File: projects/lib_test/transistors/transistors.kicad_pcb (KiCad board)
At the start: 2 copper layers, 21 x 16 mm, 4 parts, among them Q1001 MMBT2222A, Q1002 AO3400A, Q1003 DMP3028LFDE, Q1004 CEM3083

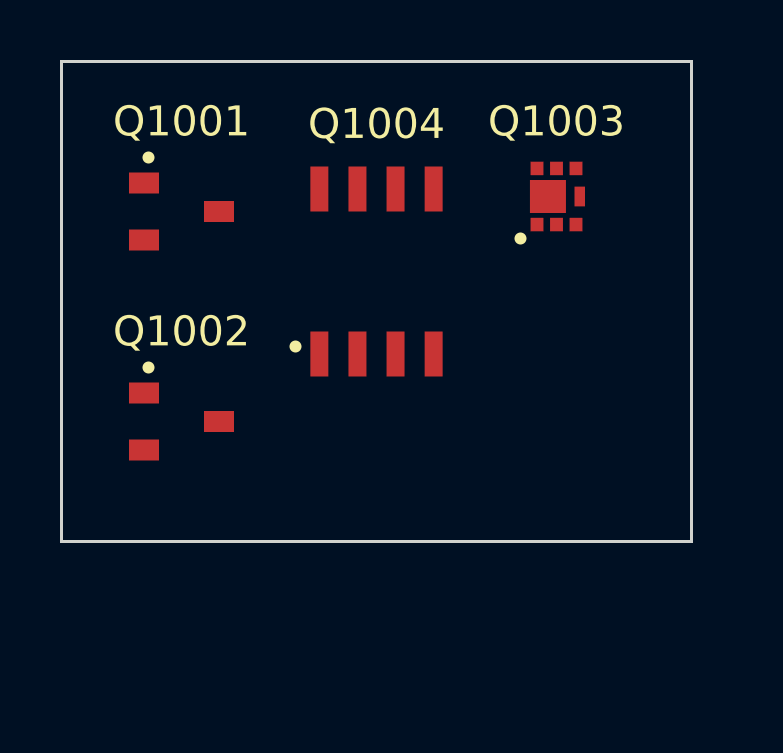
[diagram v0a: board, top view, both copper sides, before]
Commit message: add MOSFET N channel in SOIC8
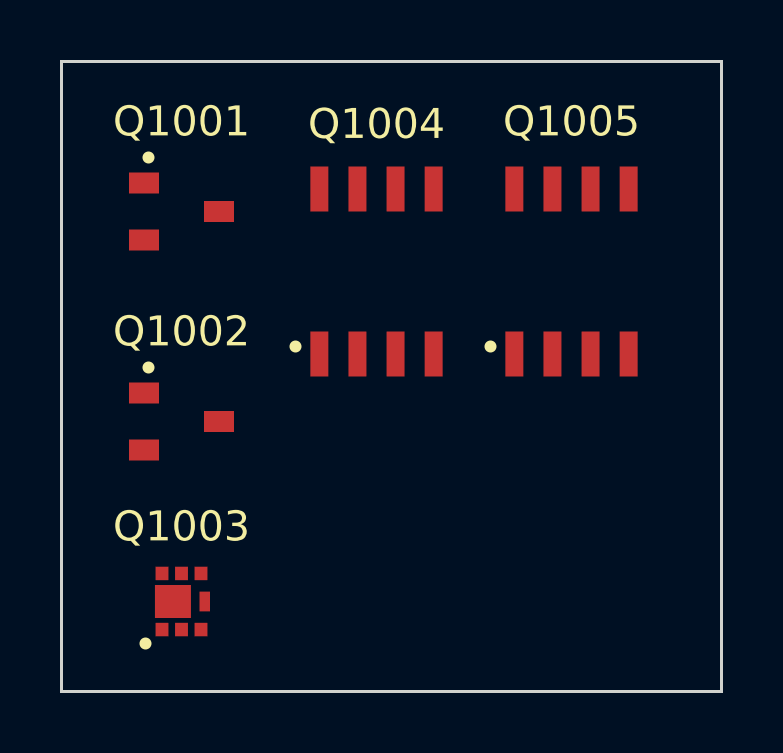
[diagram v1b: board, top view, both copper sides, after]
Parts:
- added Q1005: mosfet_n_8p_soic8, lily_footprints:soic8, F.Cu at (127.0, 77.0)
- moved Q1003 18.4 mm to (114.0, 88.0)
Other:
- board size 21 x 16 mm -> 22 x 21 mm

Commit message: updated value of N channel MOSFET
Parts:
- Q1005: value mosfet_n_8p_soic8 -> VBZA4800
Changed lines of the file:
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@@
 			)
 		)
-		(property "Value" "mosfet_n_8p_soic8"
+		(property "Value" "VBZA4800"
 			(at 0 0 0)
 			(unlocked yes)

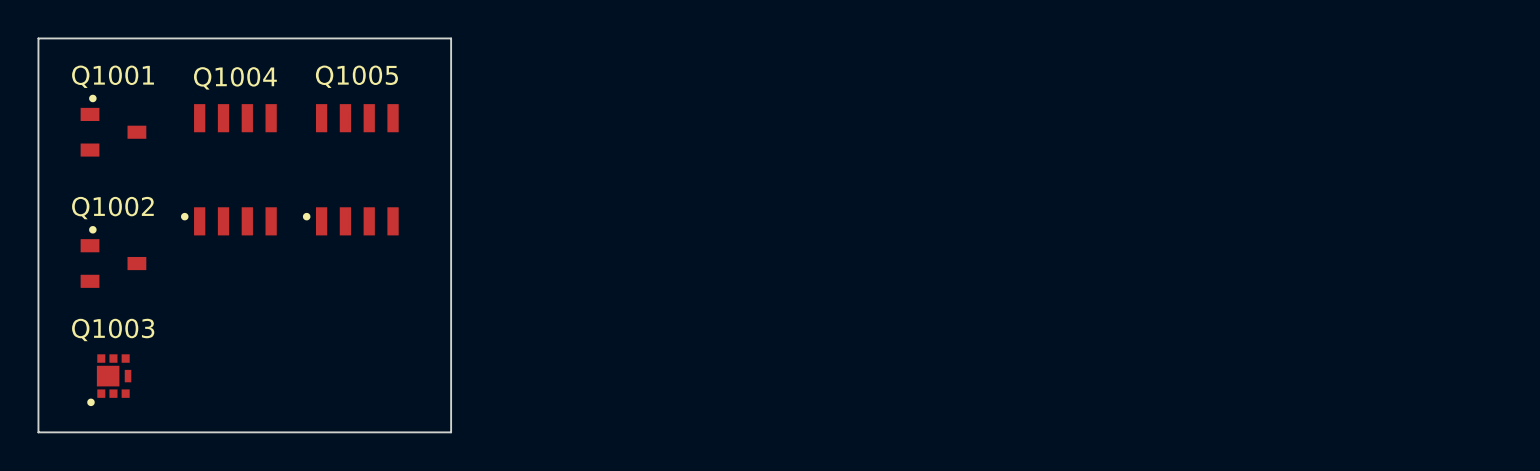
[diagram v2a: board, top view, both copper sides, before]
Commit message: add transistors to the test design
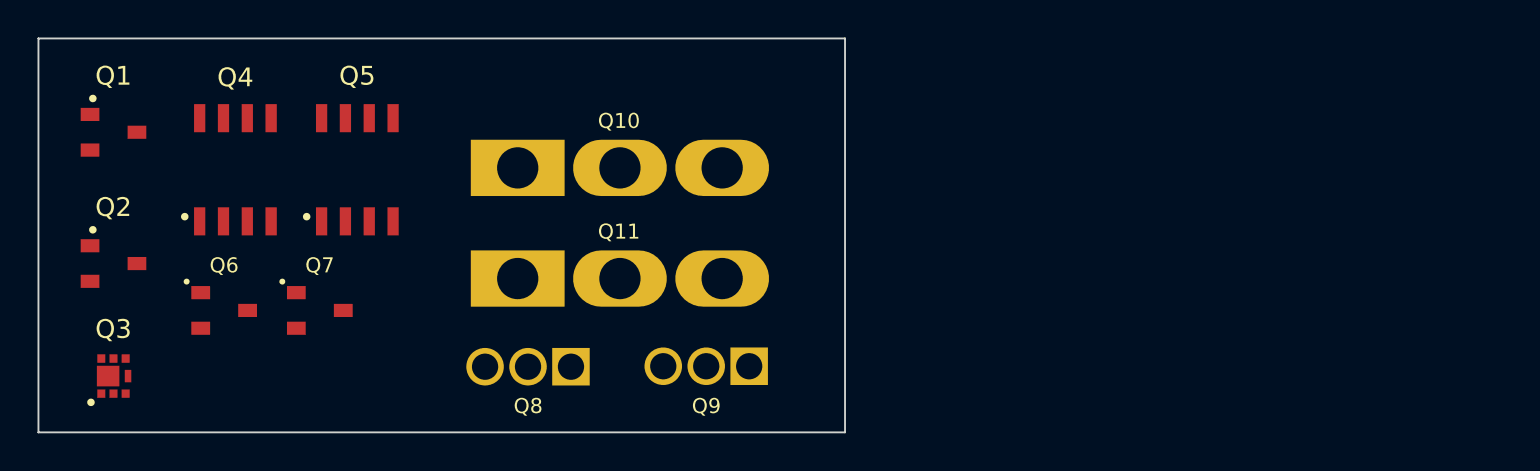
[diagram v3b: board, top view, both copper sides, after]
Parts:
- added Q10: MJL3281A, lily_footprints:to264, F.Cu at (135.6, 76.9)
- added Q11: MJL1302A, lily_footprints:to264, F.Cu at (135.6, 82.8)
- added Q6: BC850B, lily_footprints:sot23, F.Cu at (119.9, 84.5)
- added Q7: BC860B, lily_footprints:sot23, F.Cu at (125.0, 84.5)
- added Q8: BD139, lily_footprints:to126, F.Cu at (133.8, 87.5)
- added Q9: BD140, lily_footprints:to126, F.Cu at (143.3, 87.5)
- renumbered Q1001 to Q1, Q1002 to Q2, Q1003 to Q3, Q1004 to Q4, Q1005 to Q5
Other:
- board size 22 x 21 mm -> 43 x 21 mm

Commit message: updated transistors test project
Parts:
- removed Q1: MMBT2222A, lily_footprints:sot23
- removed Q2: AO3400A, lily_footprints:sot23
- removed Q4: CEM3083, lily_footprints:soic8
- removed Q5: VBZA4800, lily_footprints:soic8
- added Q1007: MMBT2222AL, lily_footprints:sot23, F.Cu at (114.0, 81.0)
- added Q1008: DMG3406L, lily_footprints:sot23, F.Cu at (119.0, 81.0)
- moved Q1006 34.9 mm to (169.6, 75.0)
- moved Q1003 16.3 mm to (124.7, 74.0)
- moved Q1004 16.0 mm to (134.7, 74.0)
- moved Q1009 13.0 mm to (125.0, 81.0)
- moved Q1005 12.1 mm to (147.6, 75.0)
- moved Q1002 12.1 mm to (119.0, 74.0), turned to 0 degrees
- moved Q1001 12.0 mm to (114.0, 74.0), turned to 0 degrees
- renumbered Q6 to Q1001, Q7 to Q1002, Q8 to Q1003, Q9 to Q1004, Q10 to Q1005, Q11 to Q1006, Q3 to Q1009
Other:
- board size 43 x 21 mm -> 78 x 17 mm
